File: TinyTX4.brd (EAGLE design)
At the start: 44 x 44 mm, 47 parts, among them IC1 ATTINY84, IC2 IC2

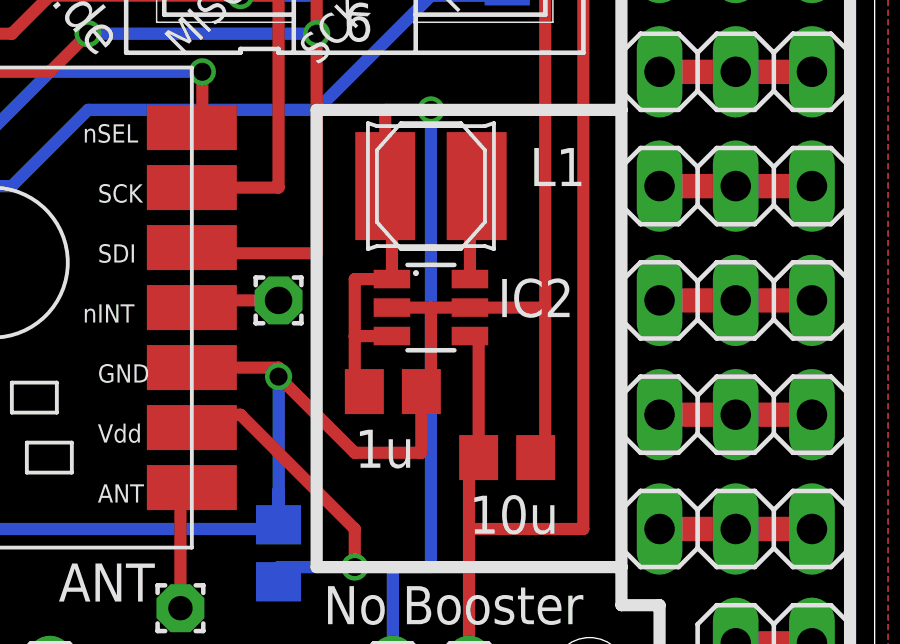
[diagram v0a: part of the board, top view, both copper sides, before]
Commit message: Update TinyTX4.brd
Fix for LTC3525 Package Size from TSOT23 to SC70
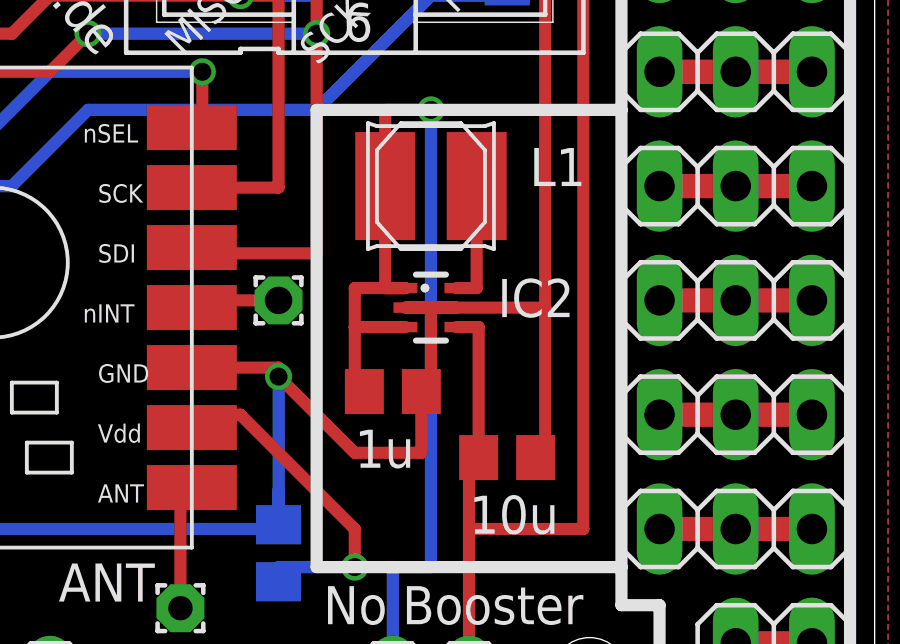
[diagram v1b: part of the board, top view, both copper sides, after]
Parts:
- IC2: device ltc3525:TSOT23-6 -> ltc3525:SC70-6
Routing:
- net V+: track 45.5 -> 46.8 mm
- net GND: track 136.6 -> 137.8 mm
- net +3V3: track 94.5 -> 95.2 mm
- net N$12: track 3.32 -> 4.08 mm
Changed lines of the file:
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@@
 <?xml version="1.0" encoding="utf-8"?>
 <!DOCTYPE eagle SYSTEM "eagle.dtd">
-<eagle version="6.4">
+<eagle version="6.5.0">
 <drawing>
 <settings>
@@
 <setting verticaltext="up"/>
 </settings>
-<grid distance="0.05" unitdist="inch" unit="mm" style="lines" multiple="1" display="yes" altdistance="0.025" altunitdist="inch" altunit="mm"/>
+<grid distance="0.635" unitdist="mm" unit="mm" style="lines" multiple="1" display="yes" altdistance="0.025" altunitdist="inch" altunit="mm"/>
 <layers>
 <layer number="1" name="Top" color="4" fill="1" visible="yes" active="yes"/>
@@
 <attribute name="NAME" x="32.5" y="19.05" size="1.27" layer="25"/>
 </element>
-<element name="IC2" library="ltc3525" package="TSOT23-6" value="IC2" x="29.21" y="15" smashed="yes" rot="R270">
+<element name="IC2" library="ltc3525" package="SC70-6" value="IC2" x="29.21" y="15" smashed="yes" rot="R270">
 <attribute name="VALUE" x="31.4325" y="14.6825" size="1.27" layer="21" ratio="10"/>
 </element>
@@
 <contactref element="SV2" pad="6"/>
 <contactref element="BATANSCHLUSS" pad="1"/>
+<contactref element="IC2" pad="2"/>
+<contactref element="C3" pad="2"/>
 <contactref element="IC2" pad="5"/>
-<contactref element="C3" pad="2"/>
-<contactref element="IC2" pad="2"/>
 <contactref element="C4" pad="2"/>
 <wire x1="29.21" y1="29.21" x2="33.02" y2="29.21" width="0.4064" layer="1"/>
@@
 <wire x1="33.02" y1="34.29" x2="35.56" y2="34.29" width="0.8128" layer="1"/>
 <wire x1="29.21" y1="35.56" x2="29.21" y2="34.29" width="0.8128" layer="1"/>
-<wire x1="30.51" y1="15" x2="33.02" y2="15" width="0.4064" layer="1"/>
-<wire x1="27.91" y1="15" x2="29.21" y2="15" width="0.4064" layer="1"/>
-<wire x1="29.21" y1="15" x2="30.51" y2="15" width="0.4064" layer="1"/>
+<wire x1="28.36" y1="15" x2="33.02" y2="15" width="0.4064" layer="1"/>
+<wire x1="30.06" y1="15" x2="29.21" y2="15" width="0.4064" layer="1"/>
+<wire x1="29.21" y1="15" x2="28.36" y2="15" width="0.4064" layer="1"/>
 <wire x1="28.89" y1="12.2" x2="29.21" y2="12.2" width="0.4064" layer="1"/>
 <wire x1="29.21" y1="12.2" x2="29.21" y2="15" width="0.4064" layer="1"/>
@@
 <wire x1="22.86" y1="11.43" x2="21.67" y2="11.43" width="0.4064" layer="1"/>
 <wire x1="21.67" y1="11.43" x2="21.24" y2="11" width="0.4064" layer="1"/>
-<wire x1="30.51" y1="14.05" x2="30.8" y2="14.05" width="0.4064" layer="1"/>
-<wire x1="30.8" y1="14.05" x2="30.8" y2="10" width="0.4064" layer="1"/>
+<wire x1="30.8" y1="14.35" x2="30.8" y2="10" width="0.4064" layer="1"/>
+<wire x1="30.06" y1="14.35" x2="30.8" y2="14.35" width="0.4064" layer="1"/>
 </signal>
 <signal name="N$8">
@@
 <contactref element="L1" pad="P$2"/>
 <contactref element="IC2" pad="6"/>
-<wire x1="30.735" y1="17.46" x2="30.735" y2="19.05" width="0.4064" layer="1"/>
-<wire x1="30.735" y1="17.46" x2="30.51" y2="17.46" width="0.4064" layer="1"/>
-<wire x1="30.51" y1="17.46" x2="30.51" y2="15.95" width="0.4064" layer="1"/>
+<wire x1="30.06" y1="15.65" x2="30.735" y2="15.65" width="0.4064" layer="1"/>
+<wire x1="30.735" y1="15.65" x2="30.735" y2="19.05" width="0.4064" layer="1"/>
 </signal>
 <signal name="V+">
@@
 <contactref element="IC2" pad="1"/>
 <contactref element="L1" pad="P$1"/>
-<wire x1="27.685" y1="17.46" x2="27.685" y2="19.05" width="0.4064" layer="1"/>
-<wire x1="27.685" y1="17.46" x2="27.91" y2="17.46" width="0.4064" layer="1"/>
-<wire x1="27.91" y1="17.46" x2="27.91" y2="15.95" width="0.4064" layer="1"/>
 <wire x1="26.67" y1="12.7" x2="26.99" y2="12.2" width="0.4064" layer="1"/>
 <contactref element="JP1" pad="2"/>
@@
 <wire x1="29.21" y1="21.59" x2="27.685" y2="21.59" width="0.4064" layer="1"/>
 <wire x1="27.685" y1="21.59" x2="27.685" y2="19.05" width="0.4064" layer="1"/>
-<wire x1="27.91" y1="13.97" x2="27.91" y2="14.05" width="0.4064" layer="1"/>
-<wire x1="27.91" y1="14.05" x2="26.67" y2="14.05" width="0.4064" layer="1"/>
-<wire x1="26.67" y1="14.05" x2="26.67" y2="12.7" width="0.4064" layer="1"/>
-<wire x1="27.91" y1="15.95" x2="26.67" y2="15.95" width="0.4064" layer="1"/>
-<wire x1="26.67" y1="15.95" x2="26.67" y2="14.05" width="0.4064" layer="1"/>
+<wire x1="26.67" y1="14.35" x2="26.67" y2="12.7" width="0.4064" layer="1"/>
+<wire x1="28.36" y1="14.35" x2="26.67" y2="14.35" width="0.4064" layer="1"/>
+<wire x1="28.36" y1="15.65" x2="26.67" y2="15.65" width="0.4064" layer="1"/>
+<wire x1="26.67" y1="15.65" x2="26.67" y2="14.35" width="0.4064" layer="1"/>
+<wire x1="28.36" y1="15.65" x2="27.685" y2="15.65" width="0.4064" layer="1"/>
+<wire x1="27.685" y1="15.65" x2="27.685" y2="19.05" width="0.4064" layer="1"/>
 </signal>
 <signal name="N$16">
